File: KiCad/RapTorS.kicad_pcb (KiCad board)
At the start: 2 copper layers, 45 x 19 mm, 27 parts, among them IC1 EFM32HG308F64G-A-QFN24, J1 Molex 48037-2200, J2 TestPoint, J3 TestPoint, J4 TestPoint, J5 TestPoint, J6 TestPoint, U2 TLV71333PDBV, U3 E07-M1101S

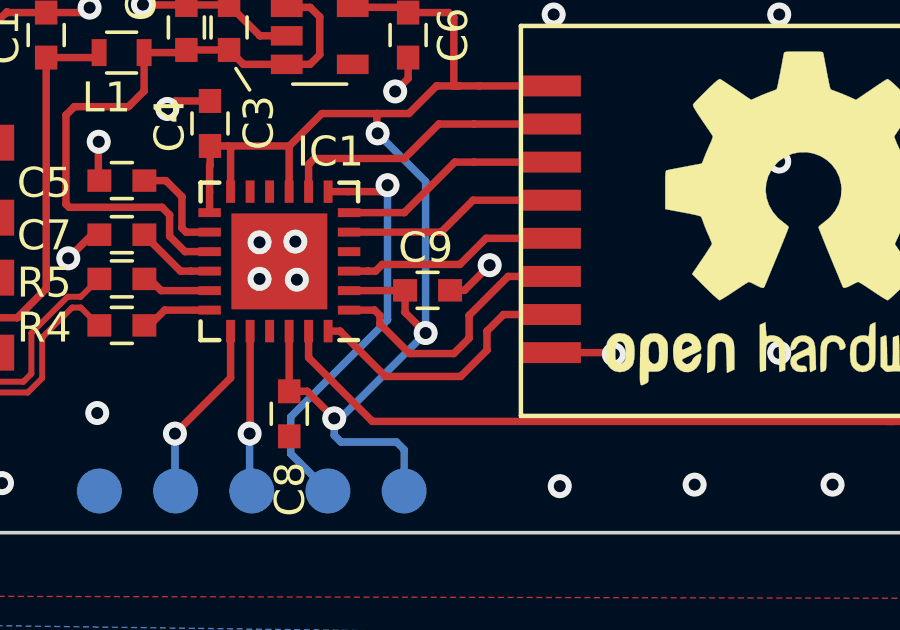
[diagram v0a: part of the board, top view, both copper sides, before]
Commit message: correct SPI pinout, add a led and a switch
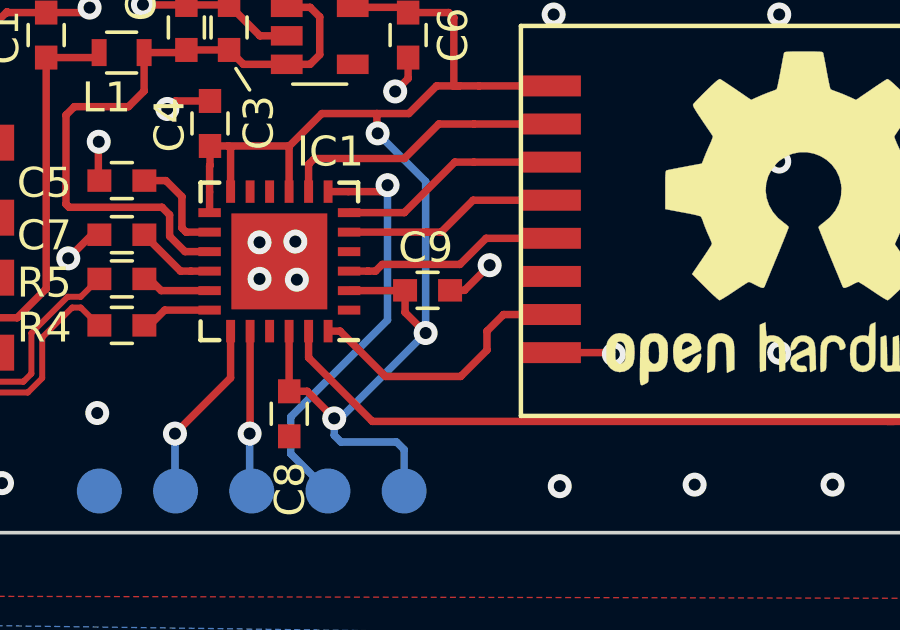
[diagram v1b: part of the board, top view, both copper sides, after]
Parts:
- R2: value 50R -> 39R
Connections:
- IC1 pad 1: MISO -> (no net)
- IC1 pad 10: Net-(IC1-Pad10) -> (no net)
- IC1 pad 11: LED_DEBUG -> (no net)
- IC1 pad 21: Net-(IC1-Pad21) -> (no net)
- IC1 pad 4: Net-(IC1-Pad4) -> MISO
- U2 pad 4: Net-(U2-Pad4) -> (no net)
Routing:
- net MISO: track 9.00 -> 0.00 mm
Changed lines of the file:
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@@
-(kicad_pcb (version 20171130) (host pcbnew "(6.0.0-rc1-dev-479-g831c9b6f6-dirty)")
+(kicad_pcb (version 20171130) (host pcbnew "(5.1.4-0-10_14)")
   (general
     (thickness 1.6)
     (drawings 20)
-    (tracks 253)
+    (tracks 244)
     (zones 0)
     (modules 27)
-    (nets 29)
+    (nets 24)
   )
   (page A4)
@@
   (net 22 SWDIO)
   (net 23 SCK)
-  (net 24 "Net-(IC1-Pad4)")
-  (net 25 "Net-(IC1-Pad10)")
-  (net 26 LED_DEBUG)
-  (net 27 "Net-(IC1-Pad21)")
-  (net 28 "Net-(U2-Pad4)")
   (net_class Default "Ceci est la Netclass par défaut."
     (clearance 0.16)
@@
     (add_net "Net-(C7-Pad1)")
     (add_net "Net-(D1-Pad2)")
+    (add_net "Net-(IC1-Pad1)")
     (add_net "Net-(IC1-Pad10)")
     (add_net "Net-(IC1-Pad17)")
     (add_net "Net-(IC1-Pad18)")
     (add_net "Net-(IC1-Pad21)")
-    (add_net "Net-(IC1-Pad4)")
     (add_net "Net-(J1-Pad5)")
     (add_net "Net-(U2-Pad4)")
@@
       (effects (font (size 1 1) (thickness 0.15)))
     )
-    (fp_text value 50R (at 0 1.5 270) (layer F.Fab)
+    (fp_text value 39R (at 0 1.5 270) (layer F.Fab)
       (effects (font (size 1 1) (thickness 0.15)))
     )
@@
     (fp_line (start 2.625 2.625) (end 2 2.625) (layer F.SilkS) (width 0.15))
     (fp_line (start 2.625 -2.625) (end 2 -2.625) (layer F.SilkS) (width 0.15))
-    (pad 1 smd rect (at -2.325 -1.625 180) (size 0.75 0.3) (layers F.Cu F.Paste F.Mask)
-      (net 17 MISO))
+    (pad 1 smd rect (at -2.325 -1.625 180) (size 0.75 0.3) (layers F.Cu F.Paste F.Mask))
     (pad 2 smd rect (at -2.325 -0.975 180) (size 0.75 0.3) (layers F.Cu F.Paste F.Mask)
       (net 1 +3V3))
@@
       (net 10 MOSI))
     (pad 4 smd rect (at -2.325 0.325 180) (size 0.75 0.3) (layers F.Cu F.Paste F.Mask)
-      (net 24 "Net-(IC1-Pad4)"))
+      (net 17 MISO))
     (pad 5 smd rect (at -2.325 0.975 180) (size 0.75 0.3) (layers F.Cu F.Paste F.Mask)
       (net 23 SCK))
@@
     (pad 9 smd rect (at -0.325 2.325 270) (size 0.75 0.3) (layers F.Cu F.Paste F.Mask)
       (net 1 +3V3))
-    (pad 10 smd rect (at 0.325 2.325 270) (size 0.75 0.3) (layers F.Cu F.Paste F.Mask)
-      (net 25 "Net-(IC1-Pad10)"))
-    (pad 11 smd rect (at 0.975 2.325 270) (size 0.75 0.3) (layers F.Cu F.Paste F.Mask)
-      (net 26 LED_DEBUG))
+    (pad 10 smd rect (at 0.325 2.325 270) (size 0.75 0.3) (layers F.Cu F.Paste F.Mask))
+    (pad 11 smd rect (at 0.975 2.325 270) (size 0.75 0.3) (layers F.Cu F.Paste F.Mask))
     (pad 12 smd rect (at 1.625 2.325 270) (size 0.75 0.3) (layers F.Cu F.Paste F.Mask)
       (net 1 +3V3))
@@
     (pad 20 smd rect (at 0.975 -2.325 270) (size 0.75 0.3) (layers F.Cu F.Paste F.Mask)
       (net 22 SWDIO))
-    (pad 21 smd rect (at 0.325 -2.325 270) (size 0.75 0.3) (layers F.Cu F.Paste F.Mask)
-      (net 27 "Net-(IC1-Pad21)"))
+    (pad 21 smd rect (at 0.325 -2.325 270) (size 0.75 0.3) (layers F.Cu F.Paste F.Mask))
     (pad 22 smd rect (at -0.325 -2.325 270) (size 0.75 0.3) (layers F.Cu F.Paste F.Mask)
       (net 1 +3V3))
@@
     (pad 3 smd rect (at -1.1 0.95) (size 1.06 0.65) (layers F.Cu F.Paste F.Mask)
       (net 2 +5V))
-    (pad 4 smd rect (at 1.1 0.95) (size 1.06 0.65) (layers F.Cu F.Paste F.Mask)
-      (net 28 "Net-(U2-Pad4)"))
+    (pad 4 smd rect (at 1.1 0.95) (size 1.06 0.65) (layers F.Cu F.Paste F.Mask))
     (pad 5 smd rect (at 1.1 -0.95) (size 1.06 0.65) (layers F.Cu F.Paste F.Mask)
       (net 1 +3V3))
@@
   (segment (start 149.4412 100.2284) (end 150.6552 101.4424) (width 0.25) (layer F.Cu) (net 16))
   (segment (start 149.4162 100.2284) (end 149.4412 100.2284) (width 0.25) (layer F.Cu) (net 16))
-  (segment (start 161.576 101.6188) (end 163.0012 101.6188) (width 0.25) (layer F.Cu) (net 17))
-  (segment (start 160.274 102.9208) (end 161.576 101.6188) (width 0.25) (layer F.Cu) (net 17))
-  (segment (start 157.1238 102.7424) (end 157.3022 102.9208) (width 0.25) (layer F.Cu) (net 17))
-  (segment (start 156.2744 102.7424) (end 157.1238 102.7424) (width 0.25) (layer F.Cu) (net 17))
-  (segment (start 157.3022 102.9208) (end 157.3022 103.2002) (width 0.25) (layer F.Cu) (net 17))
-  (segment (start 157.3022 103.2002) (end 158.2928 104.1908) (width 0.25) (layer F.Cu) (net 17))
-  (segment (start 158.2928 104.1908) (end 159.766 104.1908) (width 0.25) (layer F.Cu) (net 17))
-  (segment (start 160.274 103.6828) (end 160.274 102.9208) (width 0.25) (layer F.Cu) (net 17))
-  (segment (start 159.766 104.1908) (end 160.274 103.6828) (width 0.25) (layer F.Cu) (net 17))
   (segment (start 155.5744 98.7924) (end 156.249 98.7924) (width 0.25) (layer F.Cu) (net 18))
   (segment (start 156.249 98.7924) (end 157.3158 98.7924) (width 0.25) (layer F.Cu) (net 18))
